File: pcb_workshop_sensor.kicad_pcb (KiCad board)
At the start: 2 copper layers, 41.3 x 47 mm, 27 parts, among them IC1 ATTINY841-SSU, J1 USB, P1 BSL, P2 BSL, P3 ISP, U1 MSP430FR5738, X1 32768Hz, X2 12MHz

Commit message: v1.0
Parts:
- added C8: 0.1µF, workshop:0603, F.Cu at (60.3, 128.3)
- added R8: 10k, workshop:0603, F.Cu at (59.1, 137.8)
- added R9: 10k, workshop:0603, F.Cu at (54.0, 137.8)
- added U2: TMP275, workshop:MSOP-8, F.Cu at (66.0, 129.5)
- BT1: moved to B.Cu
- C2, C4, C6, R7, U1: moved to F.Cu
- D2, D3: footprint Diodes_ThroughHole:Diode_DO-41_SOD81_Horizontal_RM10 -> workshop:Diode-SMA_Standard
- moved C4 29.9 mm to (67.9, 149.2), turned to 90 degrees
- moved C6 25.3 mm to (64.1, 149.2), turned to 90 degrees
- moved C2 24.5 mm to (51.4, 146.1), turned to 90 degrees
- moved P3 24.3 mm to (64.8, 166.4), turned to 270 degrees
- moved X1 23.8 mm to (66.0, 146.7), turned to 180 degrees
- moved U1 21.1 mm to (56.5, 143.5), turned to 90 degrees
- moved D1 20.4 mm to (35.6, 172.7)
- moved C5 20.2 mm to (45.7, 172.7), turned to 0 degrees
- moved BT1 19.7 mm to (56.5, 139.1), turned to 45 degrees
- moved R7 19.3 mm to (48.3, 146.1), turned to 270 degrees
- moved R4 15.7 mm to (40.6, 172.7), turned to 180 degrees
- moved X2 14.9 mm to (52.1, 166.4), turned to 90 degrees
- moved R1 13.7 mm to (35.6, 170.2)
- moved P2 13.4 mm to (56.5, 151.8), turned to 0 degrees
- moved D3 10.3 mm to (30.5, 162.6), turned to 90 degrees
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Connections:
- U1 pad 22: (no net) -> /SDA
- U1 pad 23: (no net) -> /SCL
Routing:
- net +BATT: track 33.6 -> 89.3 mm, vias 1 -> 5
- net VCC: track 65.8 -> 95.0 mm
- net /AVR_RST: track 30.1 -> 59.1 mm, vias 1 -> 0
- net /MOSI: track 6.89 -> 32.4 mm
- net GND: track 9.88 -> 34.9 mm, vias 3 -> 10
- net /SCL: track 0.00 -> 24.4 mm
- net /SDA: track 0.00 -> 22.3 mm
- net /AVR_RX: track 78.2 -> 57.1 mm, vias 0 -> 1
- net /MISO: track 8.91 -> 29.6 mm, vias 0 -> 1
- net /AVR_TX: track 99.8 -> 81.2 mm
- net /SCK: track 11.1 -> 26.0 mm
- net /AVR_DTR: track 79.7 -> 66.9 mm, vias 0 -> 1
- net Net-(J1-Pad3): track 4.09 -> 15.1 mm
- net Net-(J1-Pad2): track 10.1 -> 17.0 mm
- net /AVR_RTS: track 79.8 -> 73.3 mm
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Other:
- board size 41.3 x 47 mm -> 49.5 x 49.5 mm
- board text added: "V1.0"
- board text removed: "V0.1"

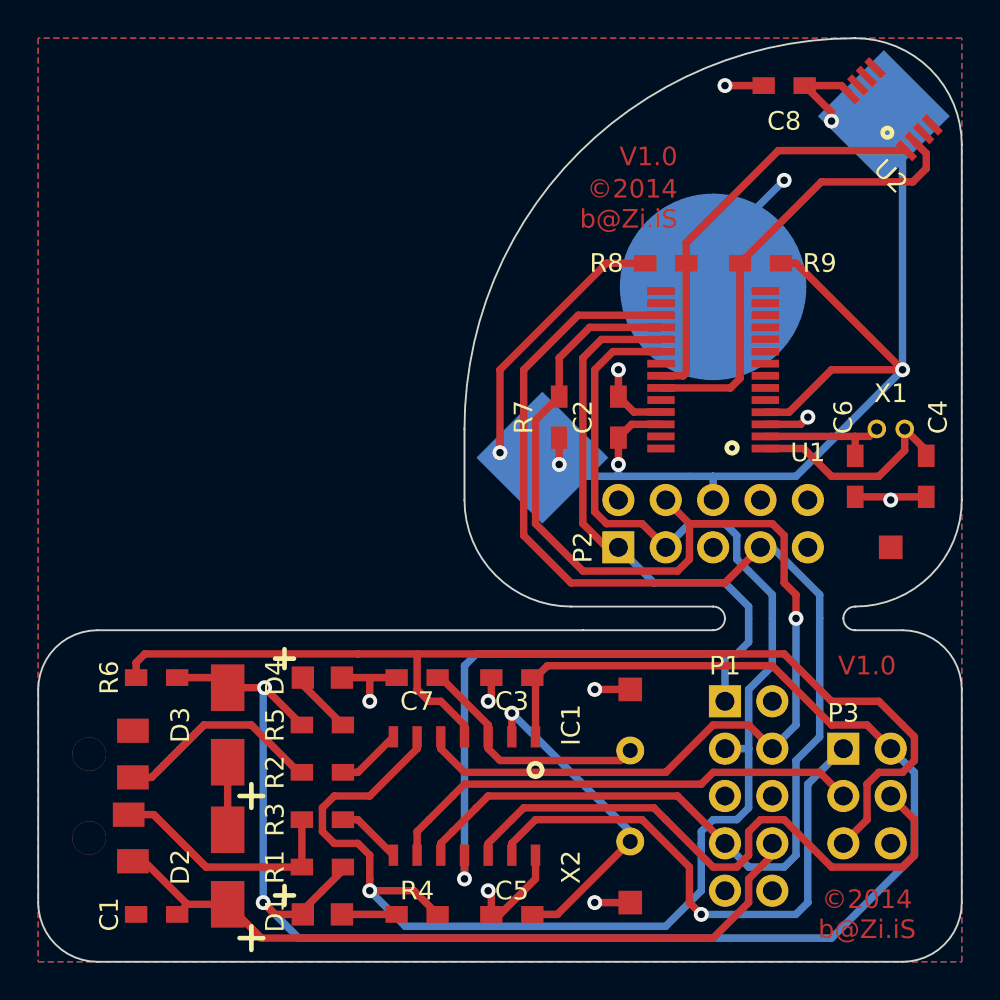
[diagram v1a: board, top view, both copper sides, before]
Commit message: repin for better layout
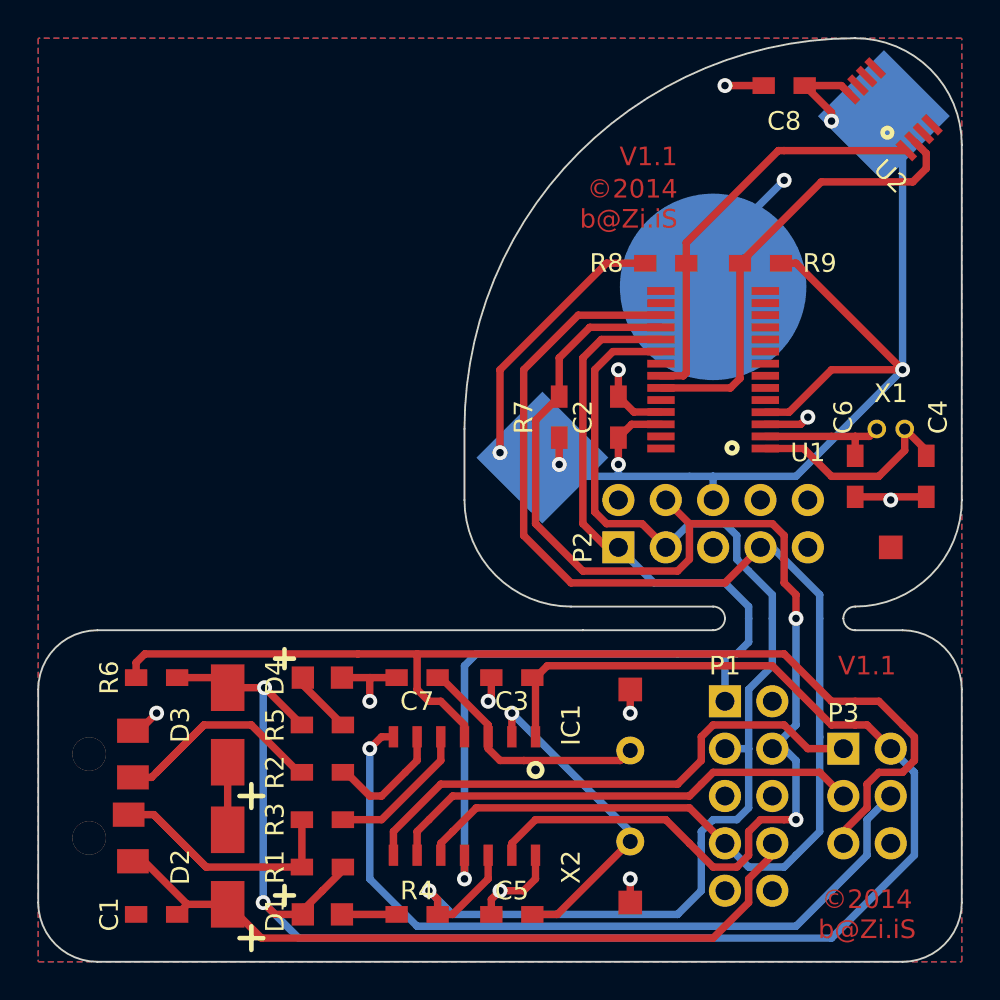
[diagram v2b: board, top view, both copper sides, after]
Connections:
- IC1 pad 12: /MOSI -> /AVR_TX
- IC1 pad 13: /MISO -> /AVR_DTR
- IC1 pad 5: /AVR_DTR -> /D-
- IC1 pad 6: /AVR_TX -> /D+
- IC1 pad 7: /D+ -> /MOSI
- IC1 pad 8: /D- -> /MISO
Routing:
- net /AVR_TX: track 81.2 -> 66.3 mm
- net /MOSI: track 32.4 -> 41.5 mm, vias 0 -> 1
- net /D-: track 3.50 -> 7.84 mm
- net /AVR_DTR: track 66.9 -> 70.3 mm, vias 1 -> 2
- net /D+: track 3.50 -> 6.57 mm
- net /AVR_RST: track 59.1 -> 58.5 mm
- net /MISO: track 29.6 -> 29.0 mm, vias 1 -> 0
- net /AVR_RTS: track 73.3 -> 72.8 mm
- net GND: track 34.9 -> 34.5 mm, vias 10 -> 11
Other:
- board text added: "V1.1"
- board text removed: "V1.0"
